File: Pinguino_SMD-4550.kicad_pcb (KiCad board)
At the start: 2 copper layers, 50.8 x 25 mm, 56 parts, among them M2,2 MountingHole_2.2mm_M2_DIN965, P1 uUSB, P10 CONN_01X01, P11 CONN_01X01, P12 CONN_01X01, P13 CONN_01X01, P14 CONN_01X01, P15 CONN_01X01, P16 CONN_01X01, P17 CONN_01X01, P18 CONN_01X01, P19 CONN_01X01, P2 CONN_01X01, P20 CONN_01X01, P21 CONN_01X01, P22 CONN_01X01, P23 CONN_01X01, P24 CONN_01X01, P25 CONN_01X01, P26 CONN_01X01, P27 CONN_01X01, P28 CONN_01X01, P29 CONN_01X01, P3 CONN_01X01, P30 CONN_01X01, P31 CONN_01X01, P32 CONN_01X01, P33 CONN_01X01, P34 CONN_01X01, P35 CONN_01X01, P36 CONN_01X01, P37 CONN_01X01, P38 CONN_01X01, P4 CONN_01X01, P5 CONN_01X01, P6 CONN_01X01, P7 CONN_01X01, P8 CONN_01X01, P9 CONN_01X01, SW1 SW Reset, U1 PIC18(L)F4550-I/PT, Y1 Crystal

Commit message: Model 3D: Case
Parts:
- added G***: LOGO, LOGO, F.Cu at (91.0, 59.4)

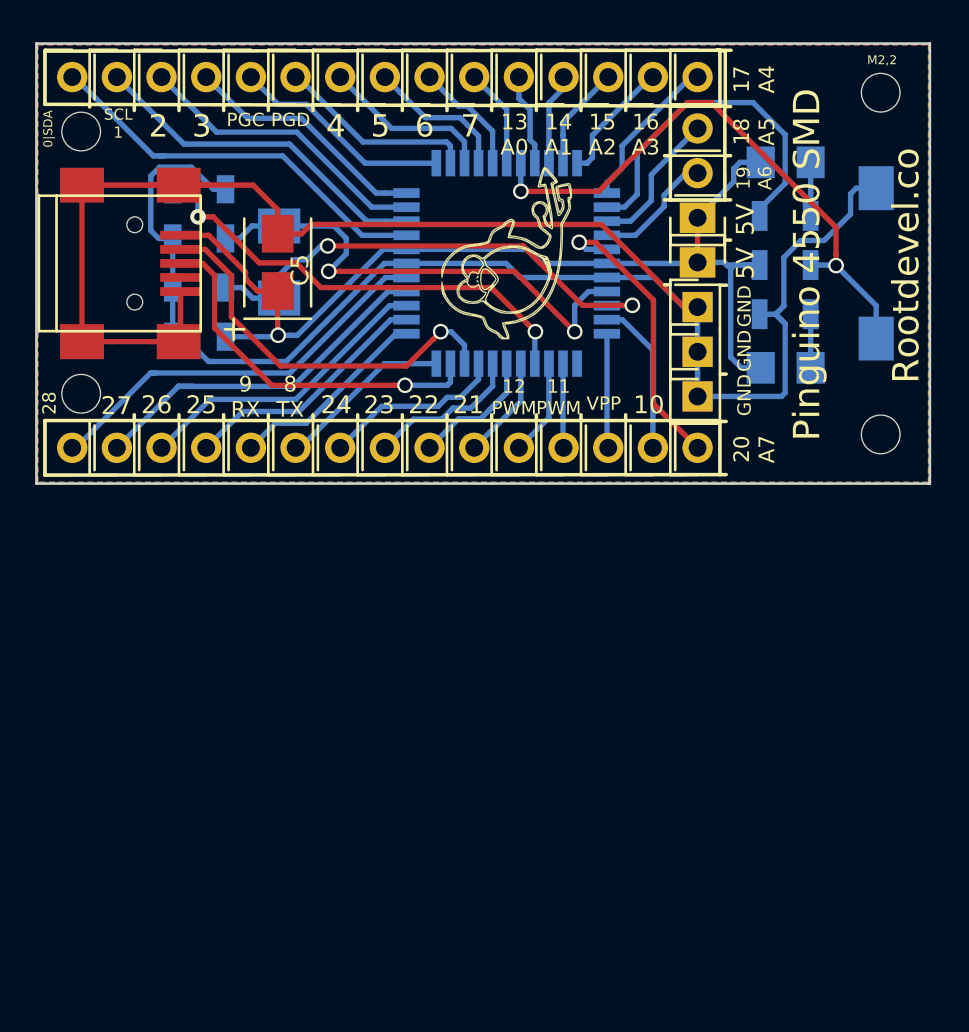
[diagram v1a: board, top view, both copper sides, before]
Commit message: Fixed Silkscreen and others. Modified readme.md file. Add Licence
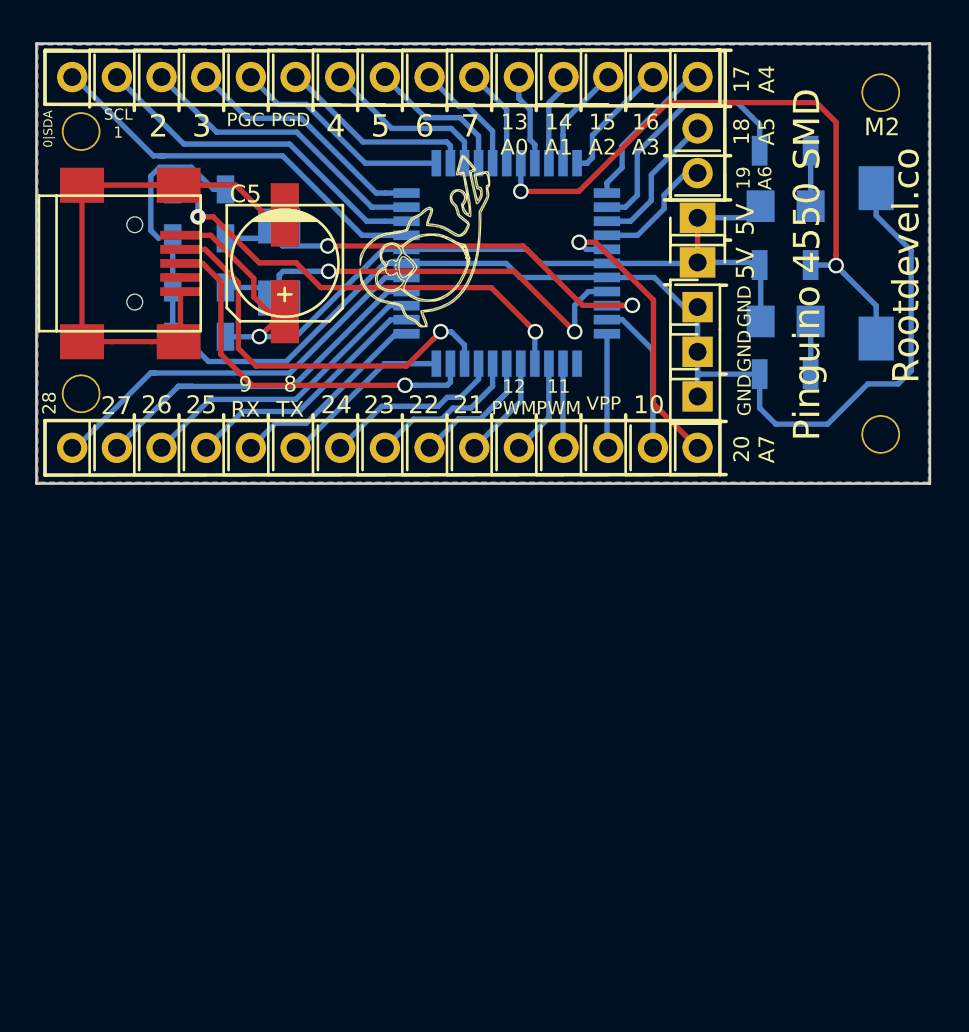
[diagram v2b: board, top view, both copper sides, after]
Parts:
- removed the G*** at (91.0, 59.4)
- removed the G*** at (66.9, 60.0)
- removed M2,2, REF** (x3): MountingHole_2.2mm_M2_DIN965, Mounting_Holes:MountingHole_2.2mm_M2_DIN965
- added G***: LOGO, LOGO, B.Cu at (66.9, 60.0)
- added G***: LOGO, LOGO, F.Cu at (86.3, 58.8)
- added M2: SolderWirePad_single_2mmDrill, Wire_Pads:SolderWirePad_single_2mmDrill, F.Cu at (66.8, 67.4)
- added M2: SolderWirePad_single_2mmDrill, Wire_Pads:SolderWirePad_single_2mmDrill, F.Cu at (66.8, 52.5)
- added M2: SolderWirePad_single_2mmDrill, Wire_Pads:SolderWirePad_single_2mmDrill, F.Cu at (112.3, 69.7)
- added M2: SolderWirePad_single_2mmDrill, Wire_Pads:SolderWirePad_single_2mmDrill, F.Cu at (112.3, 50.3)
- C5: footprint Capacitors_Tantalum_SMD:TantalC_SizeB_EIA-3528_Wave -> Capacitors_SMD:c_elec_6.3x5.3
- D1: value Run_LED -> Run
- D2: value Power_LED -> Power
- SW1: value SW Reset -> Reset
- moved R1 3.71 mm to (106.8, 53.6)
- moved R3 3.41 mm to (106.8, 66.3)
- moved C1 2.80 mm to (73.5, 58.6)
- moved C2 2.79 mm to (73.5, 61.4)
- moved D2 2.64 mm to (106.9, 63.3)
- moved D1 2.49 mm to (106.9, 56.7)
- moved C5 0.41 mm to (78.4, 60.0), turned to 270 degrees
- turned Y1 to 90 degrees
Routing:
- net GND: track 136.4 -> 112.9 mm
- net VCC: track 60.2 -> 53.4 mm
- net /RA4: track 20.0 -> 14.6 mm
- net /MCLR: track 33.3 -> 36.8 mm
- net /OSC1: track 28.8 -> 26.6 mm
- net /OSC0: track 28.2 -> 27.3 mm
- net /D-: track 22.5 -> 23.3 mm
- net /D+: track 21.1 -> 21.8 mm
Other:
- net class Default: clearance 0.3048 -> 0.508
- rule trace_clearance: 0.3048 -> 0.508

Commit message: Reorganized and aligned components.
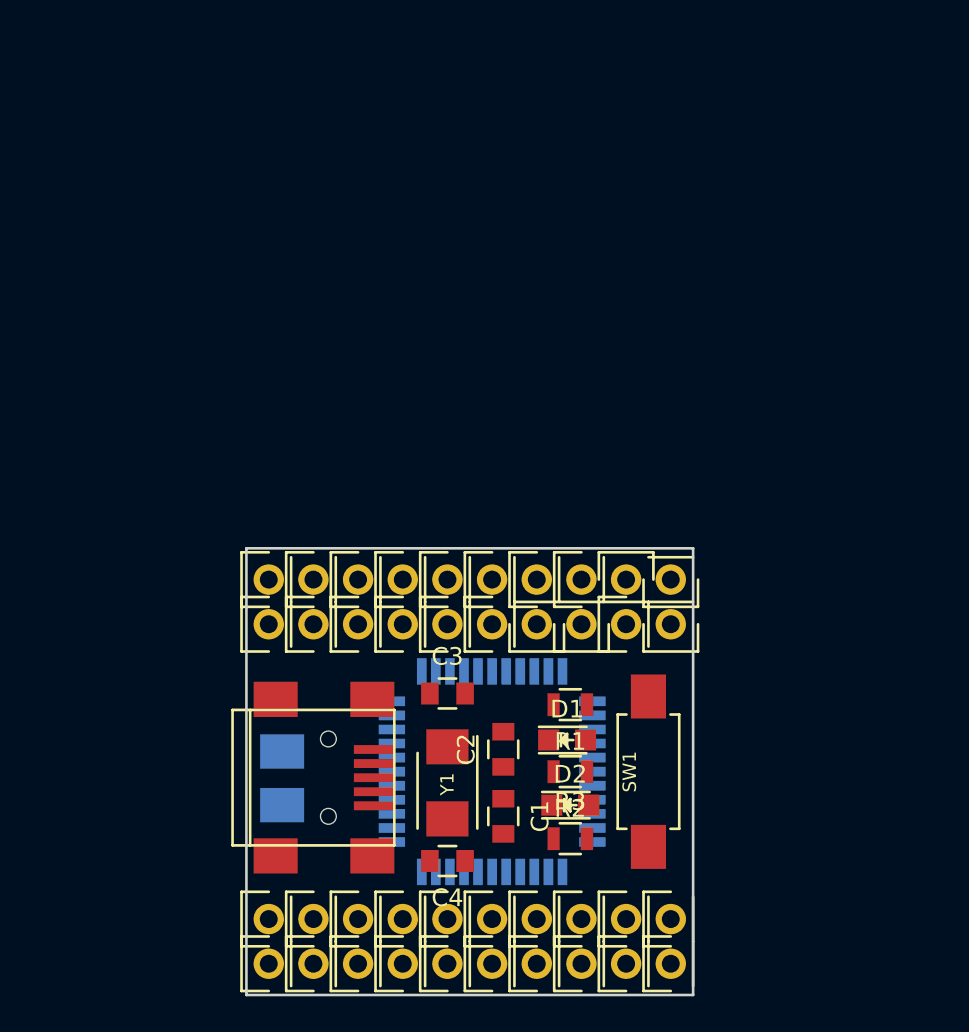
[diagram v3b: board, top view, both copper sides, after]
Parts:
- removed G*** (x2): LOGO, LOGO
- removed M2 (x4): SolderWirePad_single_2mmDrill, Wire_Pads:SolderWirePad_single_2mmDrill
- added P39: CONN_01X01, Socket_Strips:Socket_Strip_Straight_1x01, F.Cu at (97.8, 97.3)
- added P40: CONN_01X01, Socket_Strips:Socket_Strip_Straight_1x01, F.Cu at (100.3, 97.3)
- added P41: CONN_01X01, Socket_Strips:Socket_Strip_Straight_1x01, F.Cu at (100.3, 80.5)
- C1, C2, C3, C4: footprint Capacitors_SMD:C_1206 -> Capacitors_SMD:C_0805; moved to F.Cu
- C5: footprint Capacitors_SMD:c_elec_6.3x5.3 -> Capacitors_Tantalum_SMD:CP_Tantalum_Case-B_EIA-3528-21_Reflow; moved to B.Cu
- D1: value Run -> Run_LED; footprint LEDs:LED_1206 -> LEDs:LED_0805; moved to F.Cu
- D2: value Power -> Power_LED; footprint LEDs:LED_1206 -> LEDs:LED_0805; moved to F.Cu
- R1, R2, R3: footprint Resistors_SMD:R_1206 -> Resistors_SMD:R_0805; moved to F.Cu
- SW1, Y1: moved to F.Cu
- moved C4 40.7 mm to (87.6, 94.0)
- moved P3 37.9 mm to (95.2, 99.8)
- moved C1 37.1 mm to (90.8, 91.4), turned to 270 degrees
- moved P5 34.8 mm to (100.3, 99.8)
- moved R1 33.8 mm to (94.6, 85.1), turned to 180 degrees
- moved D1 32.8 mm to (94.4, 87.1), turned to 0 degrees
- moved P38 32.5 mm to (97.8, 99.8)
- moved P10 32.4 mm to (90.2, 80.5)
- moved P33 31.8 mm to (87.6, 80.5)
- moved SW1 31.7 mm to (99.1, 88.9), turned to 270 degrees
- moved C2 31.4 mm to (90.8, 87.6), turned to 90 degrees
- moved P34 31.4 mm to (77.5, 99.8)
- moved P12 31.4 mm to (97.8, 80.5)
- moved P19 31.4 mm to (85.1, 80.5)
- moved R2 31.3 mm to (94.6, 88.9), turned to 180 degrees
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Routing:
- net GND: track 112.9 -> 0.00 mm
- net VCC: track 53.4 -> 0.00 mm, vias 1 -> 0
- net /MCLR: track 36.8 -> 0.00 mm, vias 2 -> 0
- net /OSC0: track 27.3 -> 0.00 mm, vias 2 -> 0
- net /OSC1: track 26.6 -> 0.00 mm, vias 2 -> 0
- net /VUSB: track 26.4 -> 0.00 mm, vias 2 -> 0
- net /PIN0/SDA: track 23.4 -> 0.00 mm
- net /D-: track 23.3 -> 0.00 mm, vias 1 -> 0
- net /PIN28: track 23.2 -> 0.00 mm
- net /D+: track 21.8 -> 0.00 mm, vias 1 -> 0
- net /PIN27: track 21.5 -> 0.00 mm
- net /PIN1/SCL: track 19.9 -> 0.00 mm
- net /PIN26: track 17.3 -> 0.00 mm
- net /PIN2: track 17.0 -> 0.00 mm
- net /PIN20/A7: track 16.8 -> 0.00 mm, vias 1 -> 0
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- removed copper zone on B.Cu, net GND
- removed copper zone on F.Cu, net GND
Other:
- board size 50.8 x 25 mm -> 25.4 x 25.4 mm
- rule trace_min: 0.3048 -> 0.2032
- board text removed: "0 SDA"
- board text removed: "0|SDA"
- board text removed: "1"
- board text removed: "10"
- board text removed: "11 PWM"
- board text removed: "12 PWM"
- board text removed: "13 A0"
- board text removed: "14 A1"
- board text removed: "15 A2"
- board text removed: "16 A3"
- board text removed: "17 A4"
- board text removed: "18 A5"
- board text removed: "19 A6"
- board text removed: "19|A6"
- board text removed: "2"
- board text removed: "20 A7"
- board text removed: "21"
- board text removed: "22"
- board text removed: "23"
- board text removed: "24"
- board text removed: "25"
- board text removed: "26"
- board text removed: "27"
- board text removed: "28"
- board text removed: "3"
- board text removed: "4"
- board text removed: "5"
- board text removed: "5V"
- board text removed: "6"
- board text removed: "7"
- board text removed: "8 TX"
- board text removed: "9 RX"
- board text removed: "GND"
- board text removed: "PGC"
- board text removed: "PGD"
- board text removed: "Pinguino 4550 SMD"
- board text removed: "Rootdevel.co"
- board text removed: "SCL 1"
- board text removed: "VPP"

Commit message: Resized Throug Hole Pads
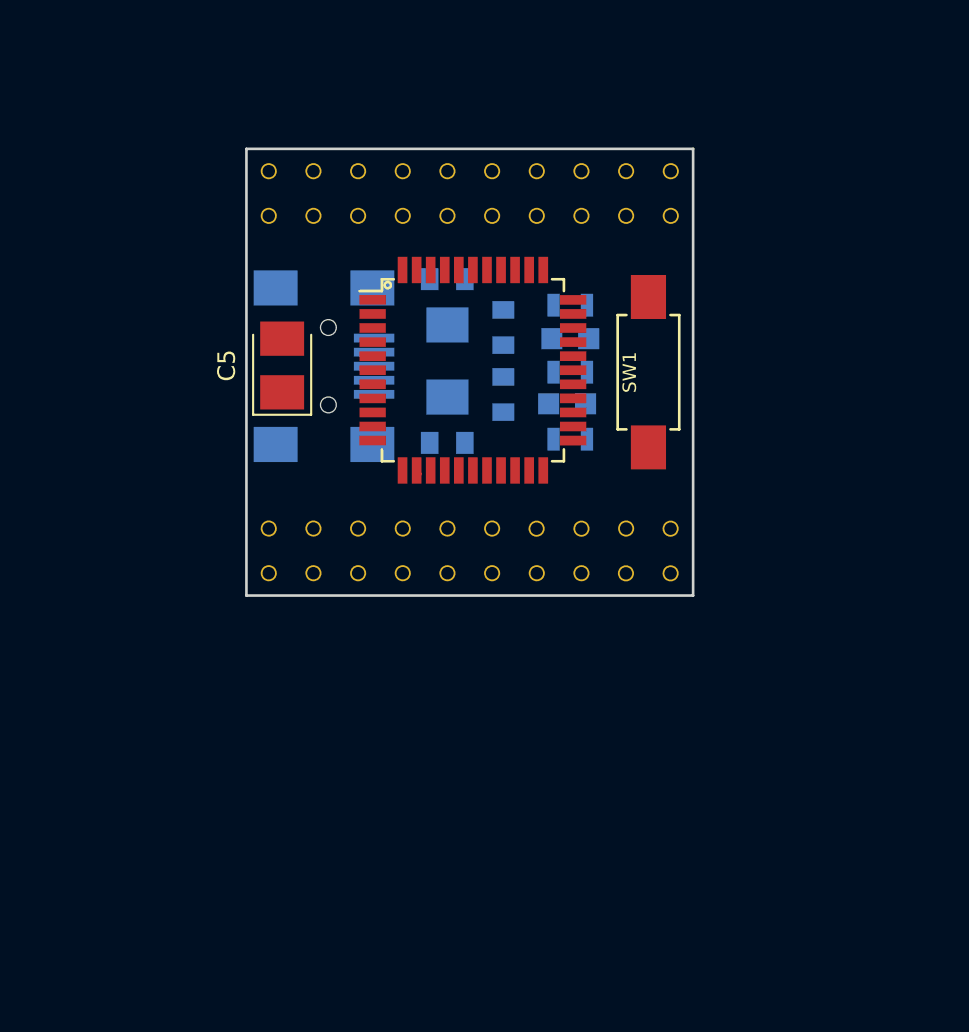
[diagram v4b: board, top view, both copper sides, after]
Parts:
- C1, C2, C3, C4, D1, D2, P1, P10, P11, P12, P13, P14, P15, P16, P17, P18, P19, P2, P20, P21, P22, P23, P24, P25, P26, P27, P28, P29, P3, P30, P31, P32, P33, P34, P35, P36, P37, P38, P39, P4, P40, P41, P5, P6, P7, P8, P9, R1, R2, R3, Y1: moved to B.Cu
- C5, U1: moved to F.Cu
- moved P21 45.1 mm to (82.5, 54.8)
- moved P22 45.1 mm to (87.6, 54.8)
- moved P24 45.1 mm to (85.1, 54.8)
- moved P25 45.1 mm to (92.7, 54.8)
- moved P27 45.1 mm to (90.2, 54.8)
- moved P3 45.1 mm to (95.2, 54.8)
- moved P30 45.1 mm to (80.0, 54.8)
- moved P34 45.1 mm to (77.5, 54.8)
- moved P38 45.1 mm to (97.8, 54.8)
- moved P5 45.1 mm to (100.3, 54.8)
- moved P18 40.0 mm to (95.2, 57.3)
- moved P20 40.0 mm to (87.6, 57.3)
- moved P23 40.0 mm to (82.5, 57.3)
- moved P26 40.0 mm to (85.1, 57.3)
- moved P28 40.0 mm to (80.0, 57.3)
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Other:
- net class Default: clearance 0.508 -> 0.254; trace_width 0.3048 -> 0.254; via_dia 0.889 -> 0.6604; via_drill 0.635 -> 0.4064
- net class Power: trace_width 0.4318 -> 0.3048; via_dia 1.397 -> 0.762; via_drill 1.016 -> 0.508
- rule trace_clearance: 0.508 -> 0.254

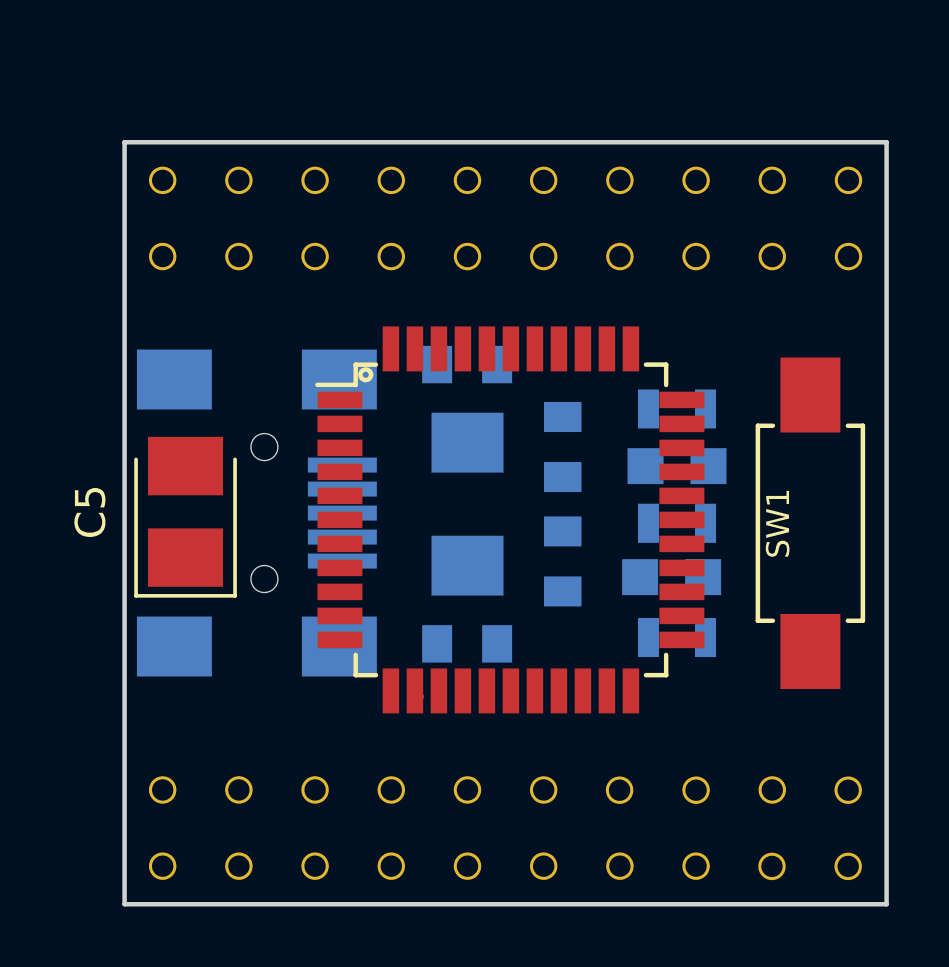
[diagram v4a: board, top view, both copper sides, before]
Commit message: Reorganized and aligned components.
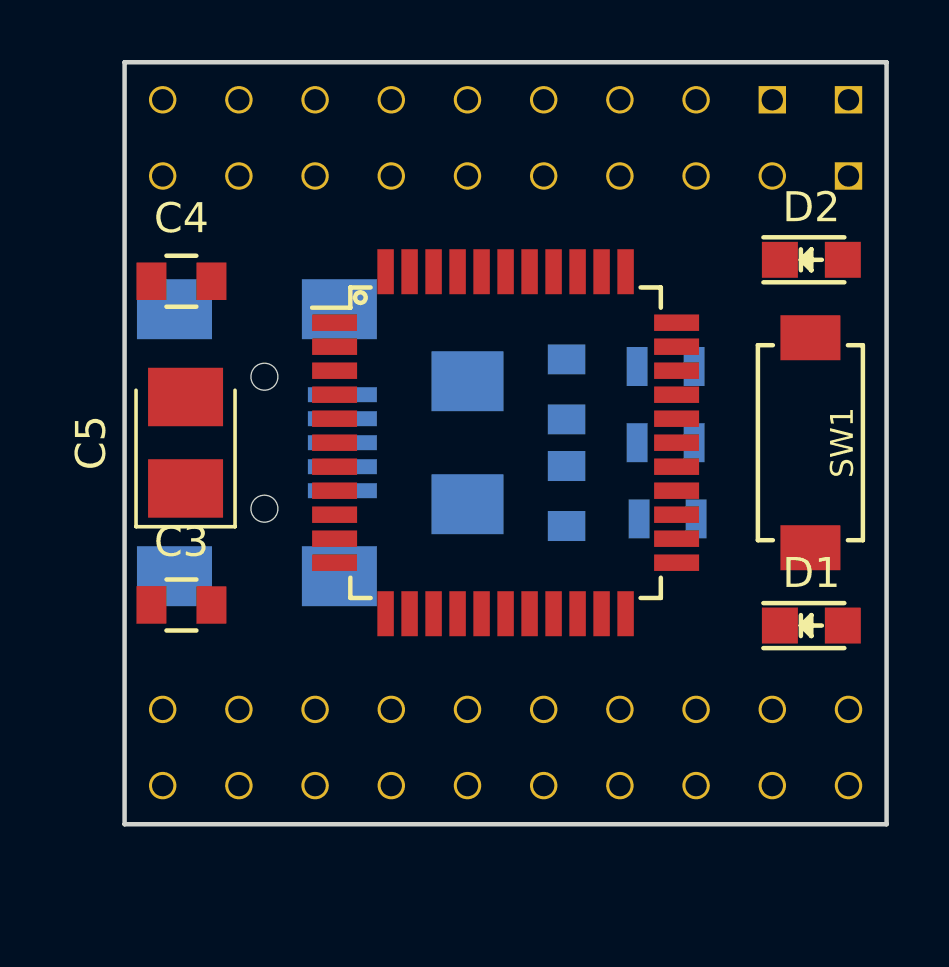
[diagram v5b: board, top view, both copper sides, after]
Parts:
- C3, C4, D1, D2: moved to F.Cu
- moved C4 9.92 mm to (78.1, 58.1), turned to 0 degrees
- moved C3 9.61 mm to (78.1, 68.9)
- moved D2 8.21 mm to (99.1, 57.4)
- moved P17 5.81 mm to (87.6, 72.4)
- moved P8 5.81 mm to (92.7, 72.4)
- moved P13 5.81 mm to (85.1, 72.4)
- moved P31 5.81 mm to (90.2, 72.4)
- moved P9 5.81 mm to (80.0, 72.4)
- moved P39 5.75 mm to (92.7, 54.6)
- moved P37 5.75 mm to (82.5, 72.4)
- moved P11 5.75 mm to (80.0, 74.9)
- moved P20 5.23 mm to (87.6, 52.1)
- moved P28 5.23 mm to (80.0, 52.1)
- moved P32 5.23 mm to (77.5, 52.1)
- moved P35 5.23 mm to (92.7, 52.1)
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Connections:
- P39 pad 1: GND -> /ICPORTS
- U1 pad 34: (no net) -> /ICPORTS

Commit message: Autoruting1, Reorganized Componets
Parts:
- moved P14 5.68 mm to (100.3, 72.4)
- moved P41 5.68 mm to (95.2, 74.9)
- moved D1 0.44 mm to (99.5, 69.6)
- moved D2 0.44 mm to (99.5, 57.4)
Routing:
- net GND: track 0.00 -> 107.7 mm, vias 0 -> 1
- net VCC: track 0.00 -> 48.1 mm
- net /MCLR: track 0.00 -> 28.1 mm, vias 0 -> 2
- net /VUSB: track 0.00 -> 22.0 mm
- net /PIN0/SDA: track 0.00 -> 19.4 mm
- net /PIN21: track 0.00 -> 17.1 mm
- net /PIN1/SCL: track 0.00 -> 14.5 mm, vias 0 -> 1
- net /PIN27: track 0.00 -> 14.5 mm
- net /PIN20/A7: track 0.00 -> 12.6 mm, vias 0 -> 1
- net /PIN26: track 0.00 -> 12.3 mm
- net /PIN28: track 0.00 -> 11.9 mm, vias 0 -> 1
- net /PIN25: track 0.00 -> 10.9 mm
- net /OSC1: track 0.00 -> 10.8 mm, vias 0 -> 1
- net /PIN19/A6: track 0.00 -> 10.2 mm
- net /PIN3: track 0.00 -> 9.41 mm
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
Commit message: Autoruting2, Reorganized Componets
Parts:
- C3, C4: moved to B.Cu
- moved C4 16.1 mm to (94.2, 57.8), turned to 180 degrees
- moved C3 16.1 mm to (94.2, 69.2)
- moved P6 3.59 mm to (80.0, 74.9)
- moved P11 2.54 mm to (80.0, 72.4)
- moved P9 2.54 mm to (77.5, 72.4)
- moved P28 2.54 mm to (80.0, 54.6)
- moved P30 2.54 mm to (80.0, 52.1)
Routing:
- net VCC: track 48.1 -> 73.5 mm
- net /VUSB: track 22.0 -> 4.57 mm, vias 0 -> 1
- net /PIN21: track 17.1 -> 6.59 mm
- net /PIN18/A5: track 0.00 -> 10.0 mm
- net GND: track 107.7 -> 97.9 mm, vias 1 -> 0
- net Net-(D1-Pad1): track 0.00 -> 5.61 mm, vias 0 -> 1
- net /PIN0/SDA: track 19.4 -> 13.8 mm, vias 0 -> 1
- net Net-(D2-Pad1): track 0.00 -> 5.38 mm, vias 0 -> 1
- net /PIN25: track 10.9 -> 7.46 mm
- net /D+: track 7.57 -> 10.7 mm
- net /MCLR: track 28.1 -> 25.5 mm
- net /PIN3: track 9.41 -> 6.87 mm
- net /PIN20/A7: track 12.6 -> 14.3 mm
- net /PIN27: track 14.5 -> 12.9 mm
- net /PIN9/RX: track 6.22 -> 5.16 mm
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
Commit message: Autoruting3
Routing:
- net /MCLR: track 25.5 -> 15.6 mm
- net VCC: track 73.5 -> 79.8 mm
- net /PIN27: track 12.9 -> 16.7 mm
- net /D+: track 10.7 -> 7.53 mm
- net GND: track 97.9 -> 95.2 mm
- net /PIN26: track 12.7 -> 11.7 mm
- net /PIN17/A4: track 6.21 -> 6.87 mm
